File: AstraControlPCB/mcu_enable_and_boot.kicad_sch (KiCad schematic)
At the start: 13 parts, among them SW1 TS_Basic_Small, SW2 TS_Basic_Small

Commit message: Update schematic titles, templates
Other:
- title: AstraControl - Root -> AstraControl - MCU Enable & Boot
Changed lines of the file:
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@@
 	(paper "A4")
 	(title_block
-		(title "AstraControl - Root")
+		(title "AstraControl - MCU Enable & Boot")
 		(date "2024-08-26")
 		(rev "A")

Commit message: Update to new rs485 chip, use 2 bit 5v gpio
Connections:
- net MCU_BOOT renamed GPIO_0_MCU_BOOT
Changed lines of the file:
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@@
 		)
 	)
-	(hierarchical_label "MCU_BOOT"
+	(hierarchical_label "GPIO_0_MCU_BOOT"
 		(shape output)
 		(at 180.34 132.08 0)

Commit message: Finished cleanup
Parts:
- added R52: 10k, LiveAstra:R_0402_1005Metric, symbol LiveAstra:R_10kOhm_0402_62mW
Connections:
- net +3V3: now also R52.1
- net GPIO_0_MCU_BOOT: now also R52.2
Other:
- moved on the sheet: R6, TP3

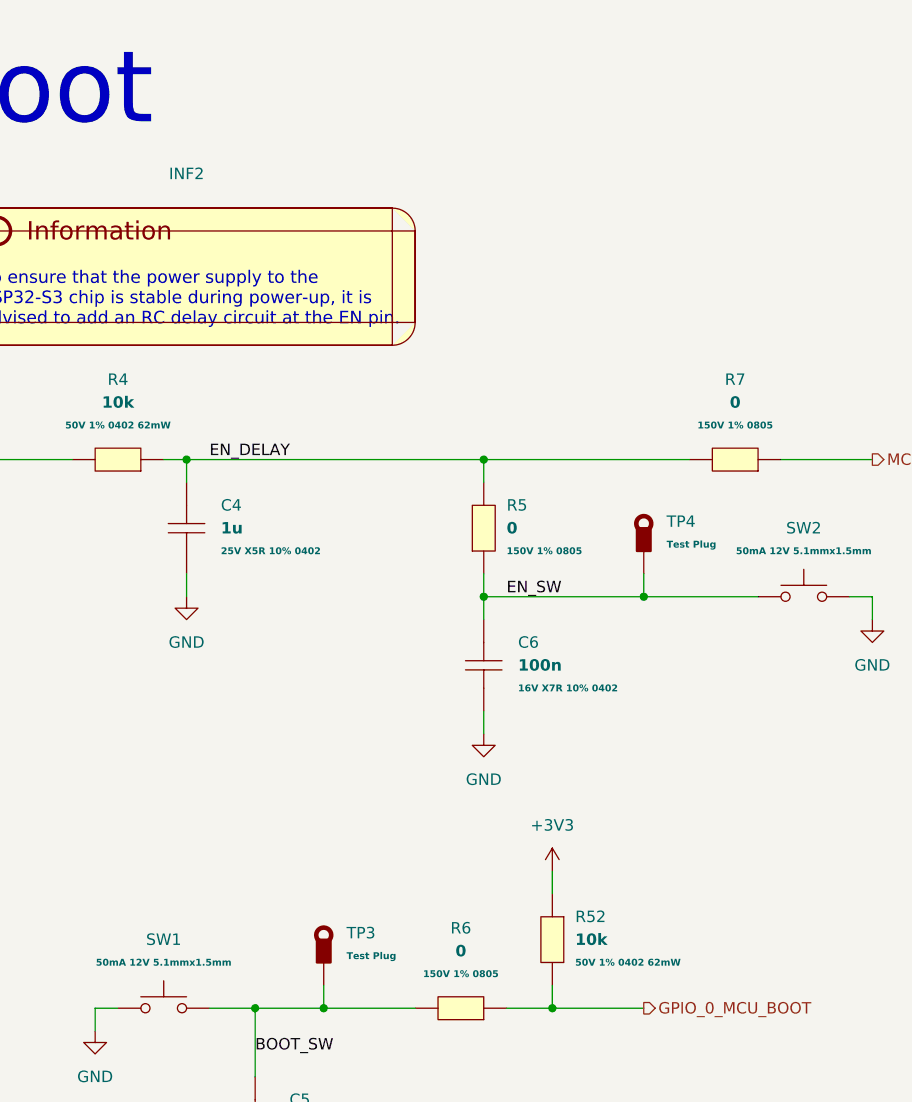
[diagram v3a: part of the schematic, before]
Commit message: New inductor that is in stock, updated rs485 ic layout to put caps closer
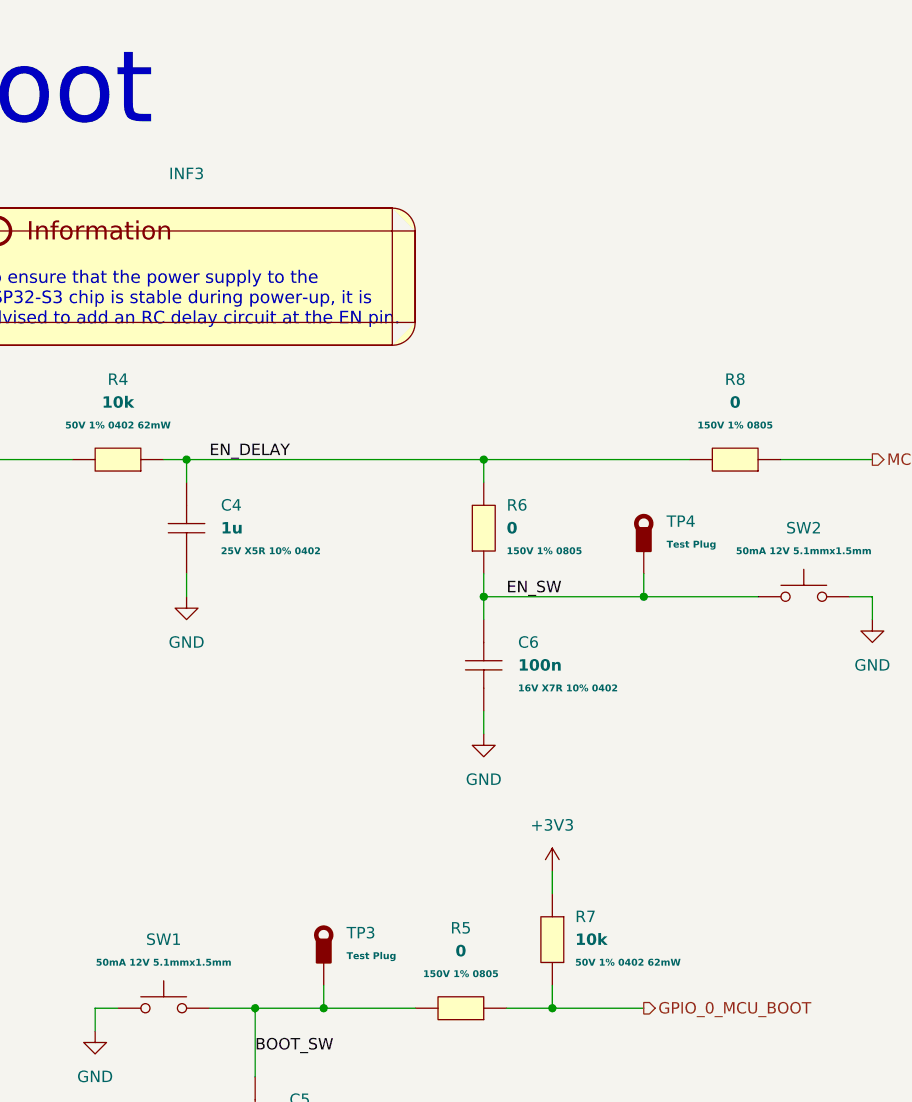
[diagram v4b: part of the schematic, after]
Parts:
- renumbered INF2 to INF3, R6 to R5, R5 to R6, R52 to R7, R7 to R8
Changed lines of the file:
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@@
 		(dnp no)
 		(fields_autoplaced yes)
-		(property "Reference" "R5"
+		(property "Reference" "R6"
 			(at 165.1 76.1999 90)
 			(effects
@@
 			(project "AstraControl"
 				(path "/9a751838-dce8-4d69-8a02-736625ac74e7/0db21d8e-3390-4d67-877f-0e5d98e37848/d7820a84-5a43-4050-a708-637b006ce625"
-					(reference "R5")
+					(reference "R6")
 					(unit 1)
 				)
@@
 		(dnp no)
 		(fields_autoplaced yes)
-		(property "Reference" "R7"
+		(property "Reference" "R8"
 			(at 190.5 62.23 0)
 			(effects
@@
 			(project "AstraControl"
 				(path "/9a751838-dce8-4d69-8a02-736625ac74e7/0db21d8e-3390-4d67-877f-0e5d98e37848/d7820a84-5a43-4050-a708-637b006ce625"
-					(reference "R7")
+					(reference "R8")
 					(unit 1)
 				)
@@
 		(dnp no)
 		(fields_autoplaced yes)
-		(property "Reference" "#PWR016"
+		(property "Reference" "#PWR017"
 			(at 205.74 95.25 0)
 			(effects
@@
 			(project "AstraControl"
 				(path "/9a751838-dce8-4d69-8a02-736625ac74e7/0db21d8e-3390-4d67-877f-0e5d98e37848/d7820a84-5a43-4050-a708-637b006ce625"
-					(reference "#PWR016")
+					(reference "#PWR017")
 					(unit 1)
 				)
@@
 		(dnp no)
 		(fields_autoplaced yes)
-		(property "Reference" "INF2"
+		(property "Reference" "INF3"
 			(at 129.54 39.37 0)
 			(effects
@@
 			(project ""
 				(path "/9a751838-dce8-4d69-8a02-736625ac74e7/0db21d8e-3390-4d67-877f-0e5d98e37848/d7820a84-5a43-4050-a708-637b006ce625"
-					(reference "INF2")
+					(reference "INF3")
 					(unit 1)
 				)
@@
 		(dnp no)
 		(fields_autoplaced yes)
-		(property "Reference" "R6"
+		(property "Reference" "R5"
 			(at 160.02 123.19 0)
 			(effects
@@
 			(project "AstraControl"
 				(path "/9a751838-dce8-4d69-8a02-736625ac74e7/0db21d8e-3390-4d67-877f-0e5d98e37848/d7820a84-5a43-4050-a708-637b006ce625"
-					(reference "R6")
+					(reference "R5")
 					(unit 1)
 				)
@@
 		(dnp no)
 		(fields_autoplaced yes)
-		(property "Reference" "#PWR096"
+		(property "Reference" "#PWR016"
 			(at 170.18 120.65 0)
 			(effects
@@
 			(project "AstraControl"
 				(path "/9a751838-dce8-4d69-8a02-736625ac74e7/0db21d8e-3390-4d67-877f-0e5d98e37848/d7820a84-5a43-4050-a708-637b006ce625"
-					(reference "#PWR096")
+					(reference "#PWR016")
 					(unit 1)
 				)
@@
 		(dnp no)
 		(fields_autoplaced yes)
-		(property "Reference" "R52"
+		(property "Reference" "R7"
 			(at 172.72 121.9199 90)
 			(effects
@@
 			(project "AstraControl"
 				(path "/9a751838-dce8-4d69-8a02-736625ac74e7/0db21d8e-3390-4d67-877f-0e5d98e37848/d7820a84-5a43-4050-a708-637b006ce625"
-					(reference "R52")
-					(unit 1)
-				)
+					(reference "R7")
+					(unit 1)
+				)

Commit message: Update revision and add year to silkscreen
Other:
- title: AstraControl - MCU Enable & Boot -> AstraControl - Root
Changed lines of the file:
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@@
 	(paper "A4")
 	(title_block
-		(title "AstraControl - MCU Enable & Boot")
+		(title "AstraControl - Root")
 		(date "2024-08-26")
-		(rev "A")
+		(rev "B")
 		(company "LiveAstra Technologies")
 	)

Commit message: Minor cleanup
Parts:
- renumbered C5 to C4, C4 to C5, R6 to R5, R5 to R6
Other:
- moved on the sheet: C4, C5, C6, R4, R5, R6, R7, SW1, SW2, TP3, TP4
